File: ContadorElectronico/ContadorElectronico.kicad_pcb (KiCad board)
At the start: 2 copper layers, 60 x 90 mm, 24 parts, among them J1 INPUT, J2 POWER, SW1 MODE, SW2 INC, SW3 DEC, U1 LM358, U3 4N35, U4 4N35

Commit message: Diseño inicial
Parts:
- added D1: 1N4002, Diode_THT:D_DO-41_SOD81_P10.16mm_Horizontal, F.Cu at (48.3, 63.5)
- added J3: Conn_01x01_Pin, Connector:Banana_Jack_1Pin, F.Cu at (37.5, 155.3)
- added J4: Conn_01x01_Pin, Connector:Banana_Jack_1Pin, F.Cu at (56.5, 155.3)
- added J5: Conn_01x01_Pin, Connector:Banana_Jack_1Pin, F.Cu at (75.6, 155.6)
- added J6: Conn_01x01_Pin, Connector:Banana_Jack_1Pin, F.Cu at (113.7, 155.6)
- added J7: Conn_01x01_Pin, Connector:Banana_Jack_1Pin, F.Cu at (32.0, 49.3)
- added J8: Conn_01x01_Pin, Connector:Banana_Jack_1Pin, F.Cu at (32.0, 64.5)
- added U6: ~, Custom:LM2596 MODULE, F.Cu at (40.6, 96.5)
- J1: value INPUT -> Screw_Terminal_01x03; footprint TerminalBlock:TerminalBlock_bornier-2_P5.08mm -> TerminalBlock:TerminalBlock_bornier-3_P5.08mm
- J2: value POWER -> Conn_01x01_Pin; footprint TerminalBlock:TerminalBlock_bornier-2_P5.08mm -> Connector:Banana_Jack_1Pin
- R1, R10, R11, R12, R2, R3, R4, R5, R6, R7, R8, R9: footprint Resistor_THT:R_Axial_DIN0207_L6.3mm_D2.5mm_P10.16mm_Horizontal -> Resistor_SMD:R_0603_1608Metric_Pad0.98x0.95mm_HandSolder
- SW1_MODE1: renamed from SW1; footprint Custom:SW Header -> Button_Switch_THT:SW_PUSH_6mm
- SW2_INC1: renamed from SW2; footprint Custom:SW Header -> Button_Switch_THT:SW_PUSH_6mm
- SW3_DEC1: renamed from SW3; footprint Custom:SW Header -> Button_Switch_THT:SW_PUSH_6mm
- U2: footprint Connector_PinSocket_2.54mm:PinSocket_1x05_P2.54mm_Vertical -> Custom:2Digit7SEG
- moved J2 101.6 mm to (94.6, 155.6)
- moved J1 94.9 mm to (88.9, 139.7), turned to 0 degrees
- moved R12 74.2 mm to (76.2, 115.5)
- moved D2 74.1 mm to (76.2, 109.2)
- moved U2 65.3 mm to (76.2, 69.8)
- moved R9 64.7 mm to (55.2, 107.3), turned to -90 degrees
- moved R1 64.2 mm to (105.4, 106.0), turned to 0 degrees
- moved A1 61.4 mm to (69.8, 125.7), turned to -90 degrees
- moved SW1_MODE1 57.1 mm to (55.2, 99.3)
- moved R3 51.6 mm to (120.7, 106.0), turned to 0 degrees
- moved R2 50.8 mm to (105.4, 108.6)
- moved R6 47.4 mm to (105.4, 127.0)
- moved R8 45.5 mm to (120.7, 129.5)
- moved R4 45.5 mm to (120.7, 108.6)
- moved R10 45.4 mm to (73.0, 107.3), turned to -90 degrees
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- renumbered D1 to D2
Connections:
- A1 pad 30: unconnected-(A1-VIN-Pad30) -> +9V
- J1 pad 1: /RESET_IN -> /NC
- J1 pad 2: /COUNT_IN -> /COM
- J2 pad 1: +5V -> /RESET_IN
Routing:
- net +5V: track 205.4 -> 74.8 mm
- net /COUNT: track 49.3 -> 2.89 mm
- net /COUNT_IN: track 13.5 -> 58.5 mm
- net GND: track 0.00 -> 45.0 mm
- net /RESET: track 39.1 -> 2.93 mm
- net /MODE_LED: track 34.8 -> 0.00 mm
- net Net-(U1A--): track 34.7 -> 6.21 mm
- net /MODE: track 26.5 -> 0.00 mm
- net Net-(U1-Pad7): track 22.3 -> 0.00 mm
- net /INC: track 21.5 -> 0.00 mm
- net /RESET_IN: track 34.3 -> 55.5 mm
- net +24V: track 0.00 -> 17.9 mm
- net /DEC: track 16.4 -> 0.00 mm
- net Net-(A1-D9): track 9.21 -> 0.00 mm
- net Net-(A1-D11): track 9.21 -> 0.00 mm
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- removed copper zone on F.Cu, net GND
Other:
- board size 60 x 90 mm -> 105.4 x 126.1 mm

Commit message: Working version #1
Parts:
- removed the J6 at (113.7, 155.6)
- removed the R1 at (105.4, 106.0)
- removed the R2 at (105.4, 108.6)
- removed the R3 at (120.7, 106.0)
- removed the R4 at (120.7, 108.6)
- removed the U1 at (109.2, 103.5)
- added J1: Conn_01x01_Pin, Connector:Banana_Jack_1Pin, F.Cu at (94.6, 155.7)
- R1: renamed from R5; value 220 -> 10k; footprint Resistor_SMD:R_0603_1608Metric_Pad0.98x0.95mm_HandSolder -> Resistor_SMD:R_1206_3216Metric_Pad1.30x1.75mm_HandSolder; moved to B.Cu
- R2: renamed from R6; value 220 -> 10k; footprint Resistor_SMD:R_0603_1608Metric_Pad0.98x0.95mm_HandSolder -> Resistor_SMD:R_1206_3216Metric_Pad1.30x1.75mm_HandSolder; moved to B.Cu
- R3: renamed from R7; footprint Resistor_SMD:R_0603_1608Metric_Pad0.98x0.95mm_HandSolder -> Resistor_SMD:R_1206_3216Metric_Pad1.30x1.75mm_HandSolder; moved to B.Cu
- R4: renamed from R8; footprint Resistor_SMD:R_0603_1608Metric_Pad0.98x0.95mm_HandSolder -> Resistor_SMD:R_1206_3216Metric_Pad1.30x1.75mm_HandSolder; moved to B.Cu
- R5: renamed from R9; footprint Resistor_SMD:R_0603_1608Metric_Pad0.98x0.95mm_HandSolder -> Resistor_SMD:R_1206_3216Metric_Pad1.30x1.75mm_HandSolder; moved to B.Cu
- R6: renamed from R10; footprint Resistor_SMD:R_0603_1608Metric_Pad0.98x0.95mm_HandSolder -> Resistor_SMD:R_1206_3216Metric_Pad1.30x1.75mm_HandSolder; moved to B.Cu
- R7: renamed from R11; footprint Resistor_SMD:R_0603_1608Metric_Pad0.98x0.95mm_HandSolder -> Resistor_SMD:R_1206_3216Metric_Pad1.30x1.75mm_HandSolder; moved to B.Cu
- R8: renamed from R12; footprint Resistor_SMD:R_0603_1608Metric_Pad0.98x0.95mm_HandSolder -> Resistor_SMD:R_1206_3216Metric_Pad1.30x1.75mm_HandSolder; moved to B.Cu
- moved J2 19.1 mm to (113.7, 156.2)
- moved R8 9.58 mm to (81.8, 107.7), turned to 90 degrees
- moved R5 4.97 mm to (50.3, 106.7), turned to 180 degrees
- moved A1 2.53 mm to (69.8, 128.3)
- moved R7 2.31 mm to (88.9, 106.7), turned to 180 degrees
- moved R1 0.99 mm to (104.4, 117.5)
- moved R2 0.99 mm to (104.4, 127.0)
- moved R3 0.99 mm to (121.6, 120.0)
- moved R4 0.99 mm to (121.6, 129.5)
- moved R6 0.43 mm to (73.2, 107.7)
- turned D2 to 0 degrees
- renumbered J1 to J3, J3 to J4, J4 to J5, J5 to J6, U2 to U1, U3 to U2, U4 to U3, U5 to U4, U6 to U5
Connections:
- net +24V renamed Net-(D1-A)
- A1 pad 10: /RELAY -> /INC
- A1 pad 11: /MODE_LED -> /MODE
- A1 pad 30: +9V -> unconnected-(A1-VIN-Pad30)
- A1 pad 5: /COUNT -> /RESET
- A1 pad 6: /RESET -> /COUNT
- A1 pad 7: /MODE -> /RELAY
- A1 pad 8: /INC -> /DEC
- A1 pad 9: /DEC -> /MODE_LED
- J2 pad 1: /RESET_IN -> /COUNT_IN
- U1 pad 3: Net-(A1-D9) -> Net-(A1-D11)
- U1 pad 5: Net-(A1-D11) -> Net-(A1-D9)
- U2 pad 1: Net-(U1-Pad1) -> /COUNT_IN
- U3 pad 1: Net-(U1-Pad7) -> /RESET_IN
- U5 pad 4: +9V -> +5V
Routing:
- net +5V: track 74.8 -> 261.0 mm
- net /COUNT: track 2.89 -> 91.2 mm
- net /RESET: track 2.93 -> 79.9 mm
- net Net-(A1-D11): track 0.00 -> 66.4 mm
- net Net-(A1-D10): track 0.00 -> 62.9 mm
- net Net-(A1-D9): track 0.00 -> 59.3 mm
- net /NC: track 0.00 -> 57.9 mm
- net /DEC: track 0.00 -> 57.8 mm
- net /MODE: track 0.00 -> 47.6 mm
- net /INC: track 0.00 -> 47.1 mm
- net /COM: track 0.00 -> 43.9 mm
- net /MODE_LED: track 0.00 -> 36.0 mm
- net /NO: track 0.00 -> 30.1 mm
- net /RELAY: track 0.00 -> 27.4 mm
- net GND: track 45.0 -> 18.6 mm
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- added copper zone on B.Cu, net GND

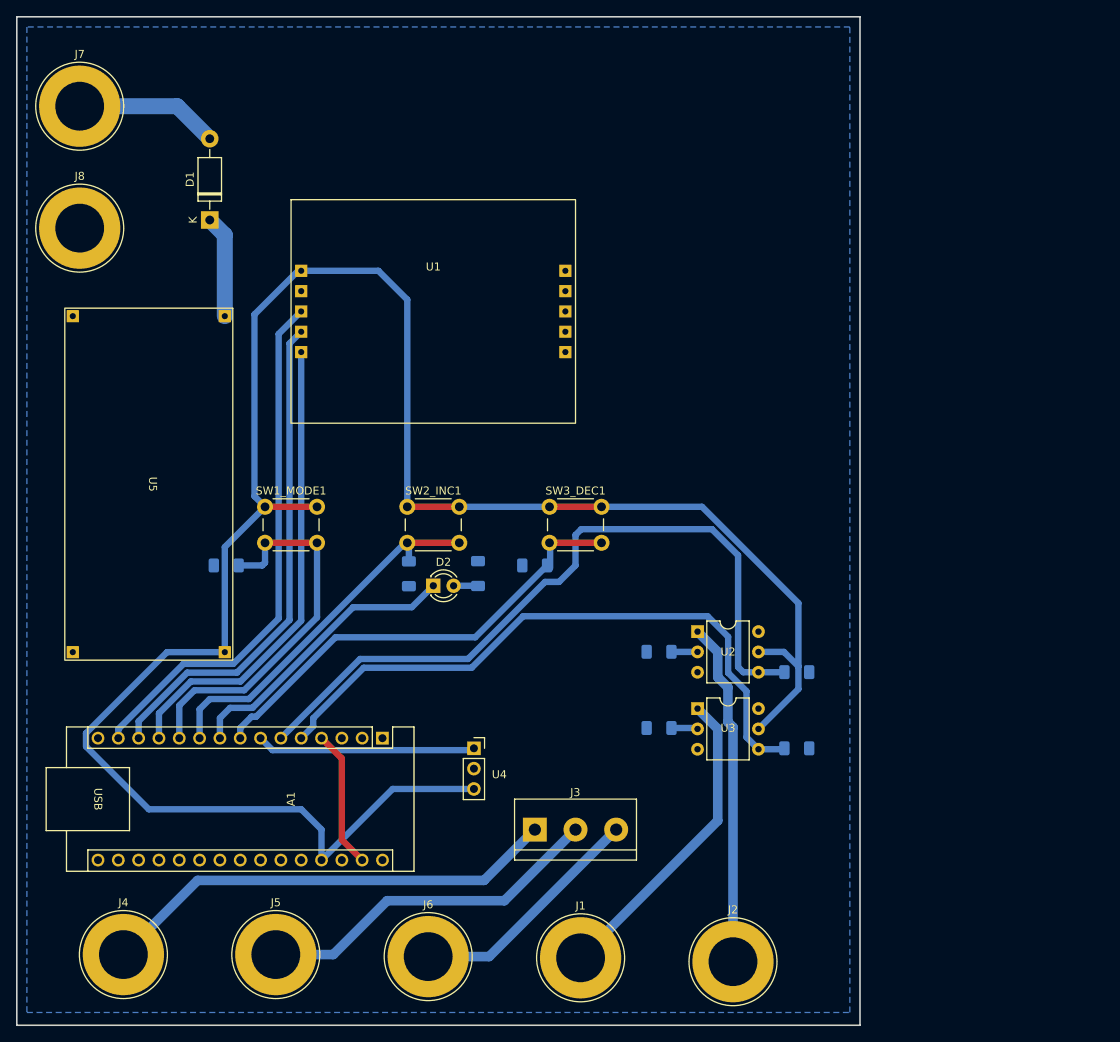
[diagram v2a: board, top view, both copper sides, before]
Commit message: ajustes a la PCB
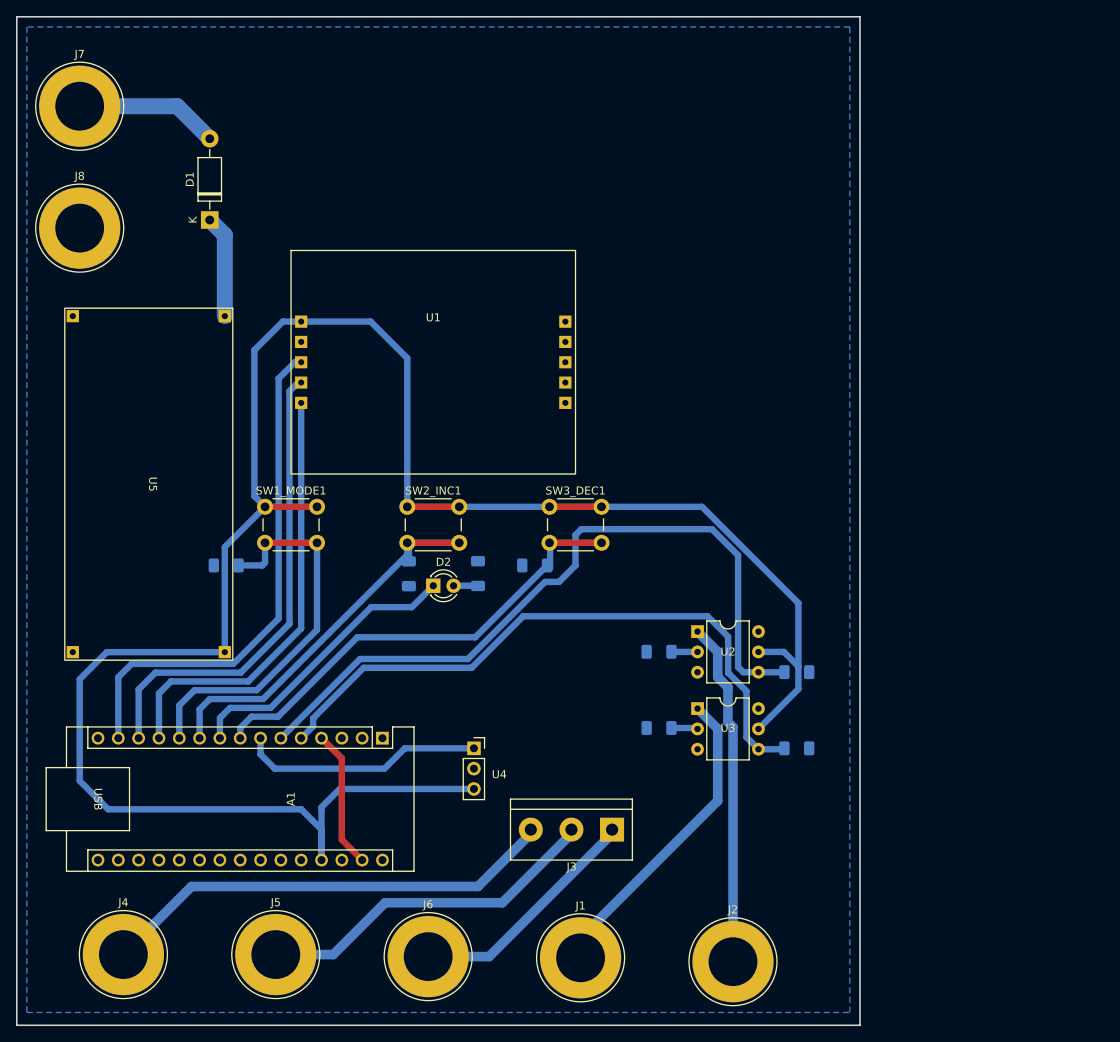
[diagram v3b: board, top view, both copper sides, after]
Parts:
- moved J3 9.65 mm to (98.6, 139.7), turned to 180 degrees
- moved U1 6.35 mm to (76.2, 76.2)
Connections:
- J4 pad 1: /NC -> /NO
- J6 pad 1: /NO -> /NC
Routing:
- net /NO: track 30.1 -> 57.9 mm
- net /NC: track 57.9 -> 30.1 mm
- net Net-(A1-D9): track 59.3 -> 54.9 mm
- net Net-(A1-D10): track 62.9 -> 59.3 mm
- net /RELAY: track 27.4 -> 30.5 mm
- net Net-(A1-D11): track 66.4 -> 64.4 mm
- net /MODE: track 47.6 -> 48.5 mm
- net /INC: track 47.1 -> 48.0 mm
